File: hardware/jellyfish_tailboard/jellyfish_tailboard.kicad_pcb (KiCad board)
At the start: 2 copper layers, 98 x 68 mm, 38 parts, among them J1 DC IN, J2 DC THRU, J3 Head, J4 Top camera, J5 8P8C_Shielded, J6 Bottom camera, J7 Bottom camera, Q1 DMP3037LSS-13

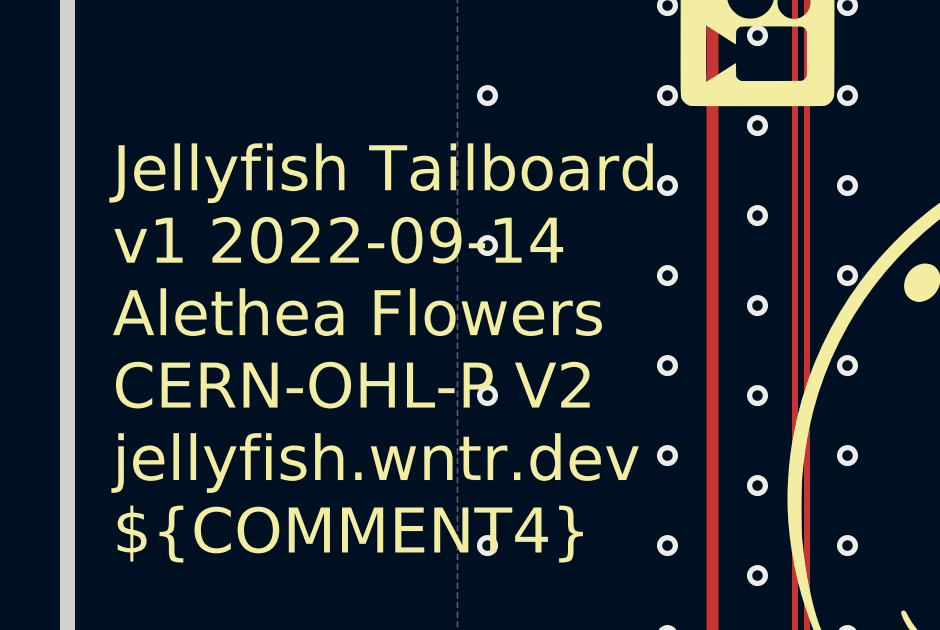
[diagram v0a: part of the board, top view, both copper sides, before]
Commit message: Update license on all hardware files
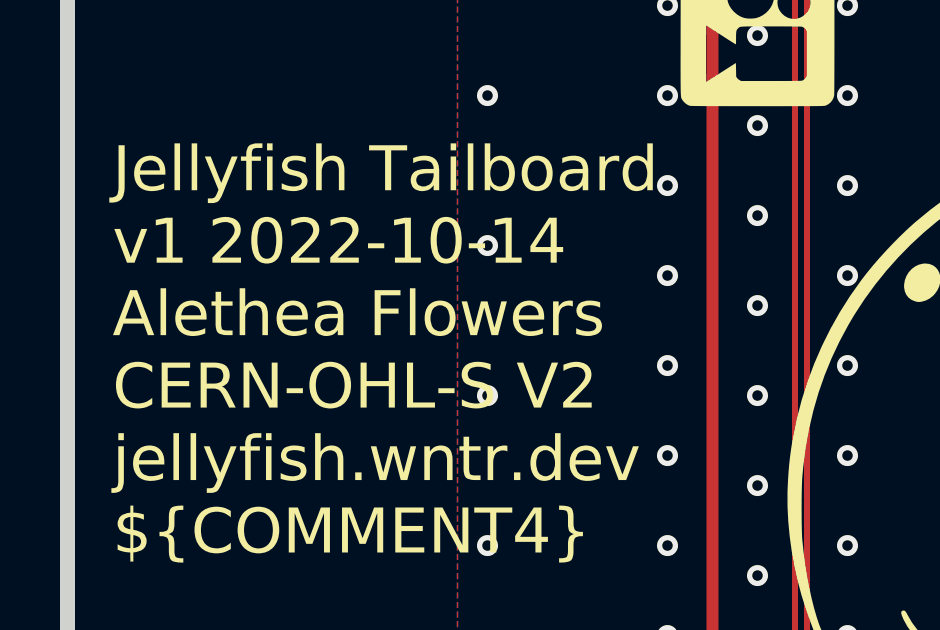
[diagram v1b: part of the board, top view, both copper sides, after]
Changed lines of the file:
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@@
   (title_block
     (title "Jellyfish Tailboard")
-    (date "2022-09-14")
+    (date "2022-10-14")
     (rev "v1")
     (company "Winterbloom")
     (comment 1 "Alethea Flowers")
-    (comment 2 "CERN-OHL-P V2")
+    (comment 2 "CERN-OHL-S V2")
     (comment 3 "jellyfish.wntr.dev")
   )
